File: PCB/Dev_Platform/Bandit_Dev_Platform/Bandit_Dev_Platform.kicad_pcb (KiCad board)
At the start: 4 copper layers, 63.5 x 31.8 mm, 136 parts, among them J1 Conn_01x03_Pin, J10 Conn_01x05_Pin, J11 Conn_01x05_Pin, J2 SMA, J3 Conn_01x05_Pin, J4 Conn_01x05_Pin, J5 BNC, J6 BNC, J8 Conn_01x05_Pin, J9 Conn_01x06_Pin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

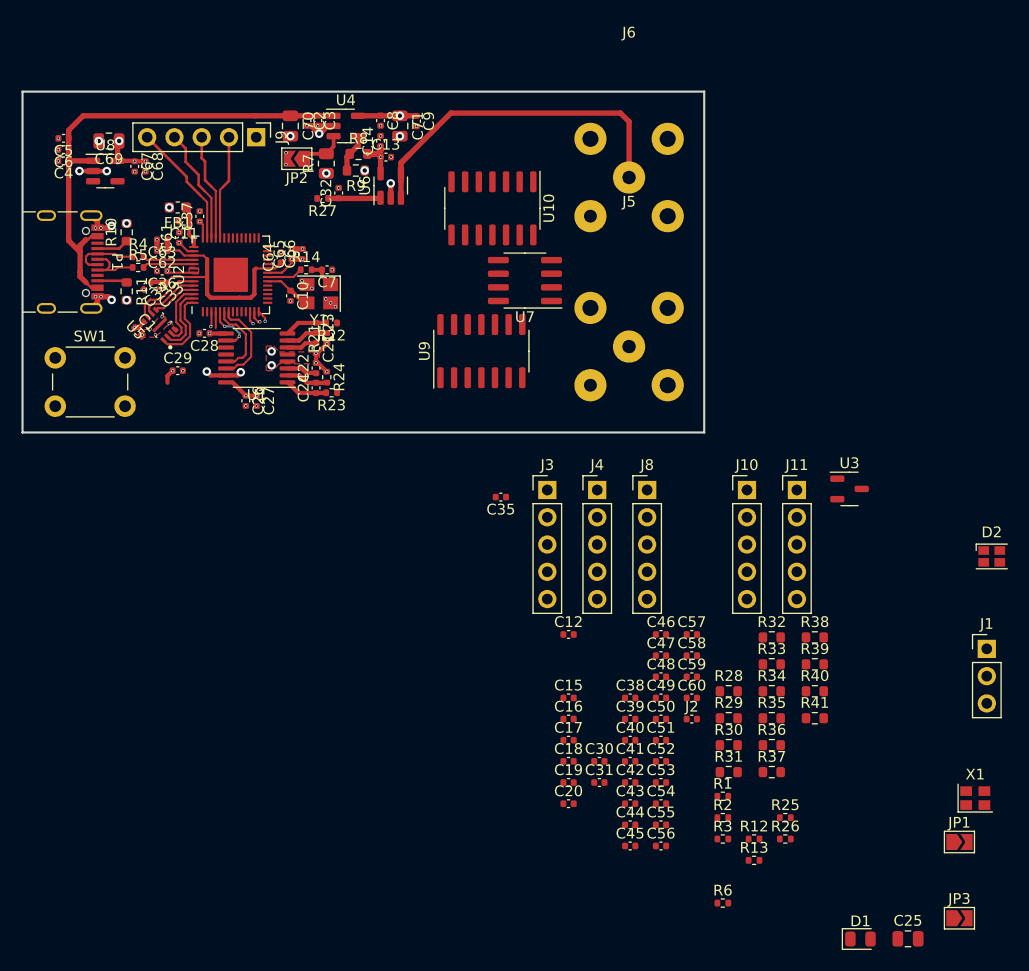
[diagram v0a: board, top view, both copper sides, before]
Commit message: Added circular buffer test, library otw
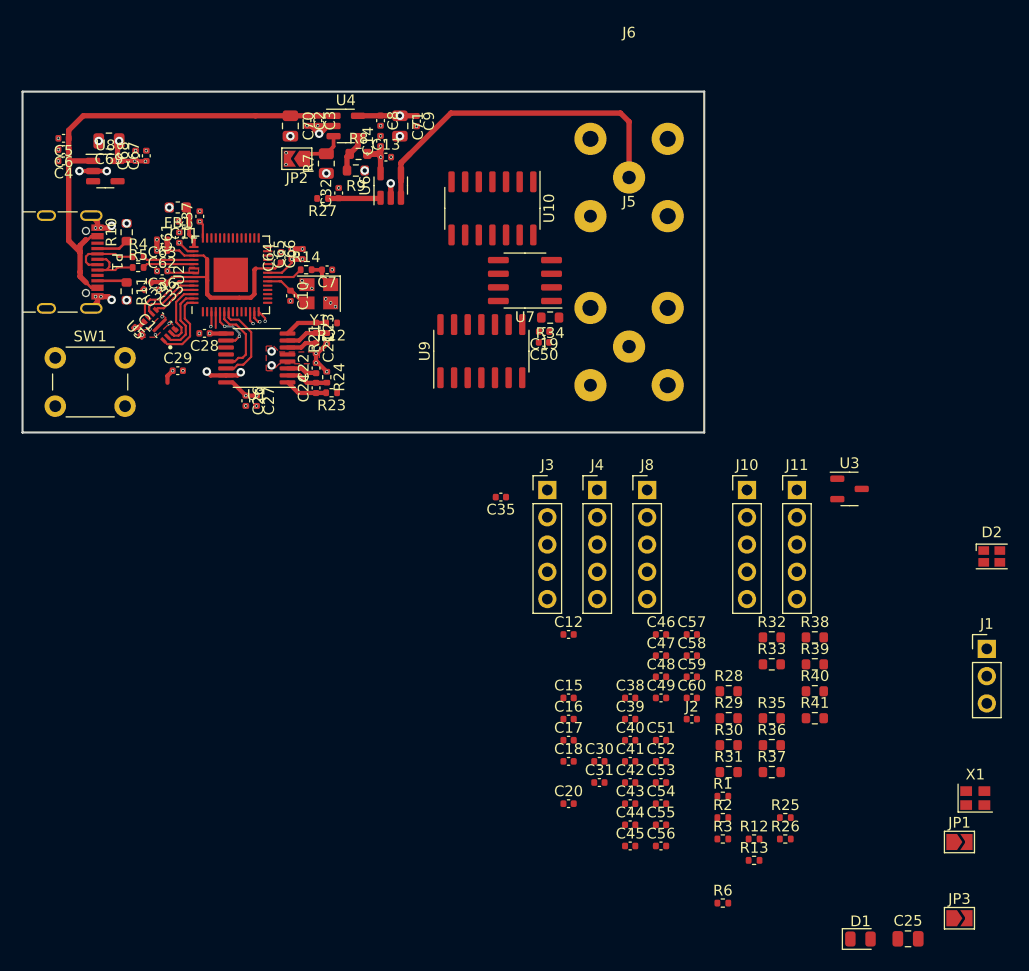
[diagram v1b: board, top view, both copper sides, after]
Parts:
- removed J9: Conn_01x06_Pin, Connector_PinHeader_2.54mm:PinHeader_1x05_P2.54mm_Vertical
- moved C19 42.1 mm to (68.6, 42.4), turned to 180 degrees
- moved R34 40.5 mm to (69.2, 41.0), turned to 180 degrees
- moved C50 36.7 mm to (68.6, 43.4), turned to 180 degrees
- moved C67 1.47 mm to (31.5, 26.0), turned to 90 degrees
- moved C68 1.35 mm to (30.5, 26.0), turned to 90 degrees
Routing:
- net Net-(J9-Pin_5): track 11.7 -> 0.00 mm
- net Net-(J9-Pin_4): track 10.8 -> 0.00 mm
- net Net-(J9-Pin_3): track 9.92 -> 0.00 mm
- net Net-(J9-Pin_2): track 9.73 -> 0.00 mm

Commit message: Circular buffers added to RP2040 evaluation stack
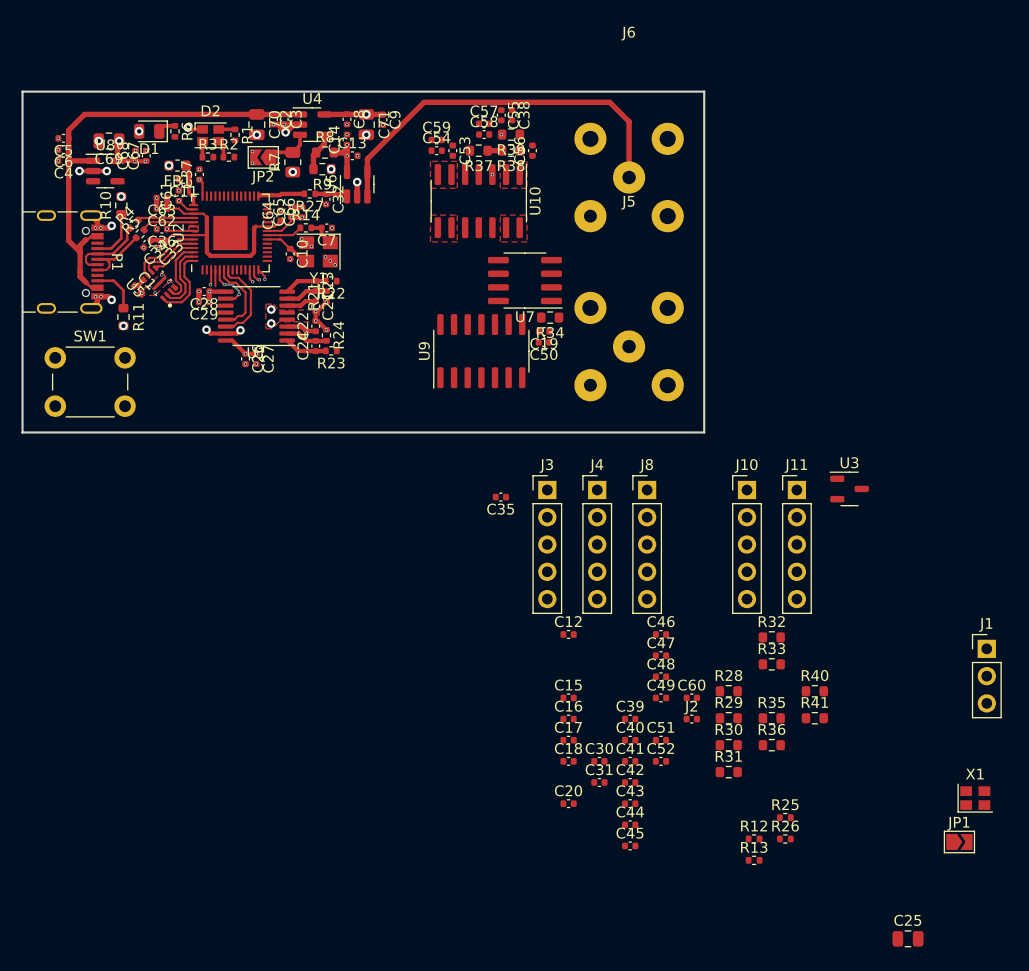
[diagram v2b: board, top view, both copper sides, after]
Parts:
- removed JP3: SolderJumper_2_Open, Jumper:SolderJumper-2_P1.3mm_Open_TrianglePad1.0x1.5mm
- moved D1 100.2 mm to (31.8, 23.7), turned to 180 degrees
- moved R6 88.2 mm to (34.2, 23.7), turned to -90 degrees
- moved D2 82.7 mm to (37.5, 24.1)
- moved R3 79.6 mm to (37.3, 26.1)
- moved R2 76.8 mm to (39.2, 26.1)
- moved R1 76.6 mm to (39.8, 24.0), turned to -90 degrees
- moved C55 67.8 mm to (64.6, 22.2), turned to -90 degrees
- moved C56 65.9 mm to (67.5, 25.5), turned to 90 degrees
- moved C54 64.3 mm to (58.6, 25.5)
- moved R37 64.0 mm to (62.5, 25.5), turned to 180 degrees
- moved C53 62.0 mm to (60.1, 25.5), turned to -90 degrees
- moved R39 56.9 mm to (65.5, 24.0), turned to 180 degrees
- moved C38 55.4 mm to (65.6, 22.2), turned to -90 degrees
- moved C59 55.4 mm to (58.6, 24.5)
- moved R38 53.4 mm to (65.5, 25.5), turned to 180 degrees
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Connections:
- P1 pad B6: (no net) -> Net-(P1-D+)
- P1 pad B7: (no net) -> Net-(P1-D-)
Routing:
- net /PDM_WGN: track 0.00 -> 4.32 mm
- net VBUS: track 46.0 -> 43.0 mm
- net /WGN_OUT: track 33.1 -> 36.0 mm
- net Net-(U6-VIN+): track 4.92 -> 3.05 mm
- net /USB_CC: track 3.01 -> 4.86 mm
- net Net-(D1-K): track 0.00 -> 1.67 mm
- net /USB_VCONN: track 2.78 -> 4.45 mm
- net Net-(D2-GK): track 0.00 -> 1.66 mm
- net Net-(D2-BK): track 0.00 -> 1.53 mm
- net Net-(D2-RK): track 0.00 -> 1.48 mm
- net Net-(C54-Pad2): track 0.00 -> 1.35 mm
- net Net-(P1-D-): track 6.24 -> 7.38 mm
- net +3V3: track 18.3 -> 19.4 mm, vias 15 -> 17
- net Net-(P1-D+): track 6.27 -> 7.33 mm
- net GND: track 21.2 -> 22.2 mm
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- added copper zone on F.Cu, net /SE_SIG_A
- added copper zone on F.Cu, net Net-(U10A--)
- added copper zone on F.Cu, net Net-(U10B--)
- added copper zone on F.Cu, net Net-(U10D--)

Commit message: Fixed filter to be cheap
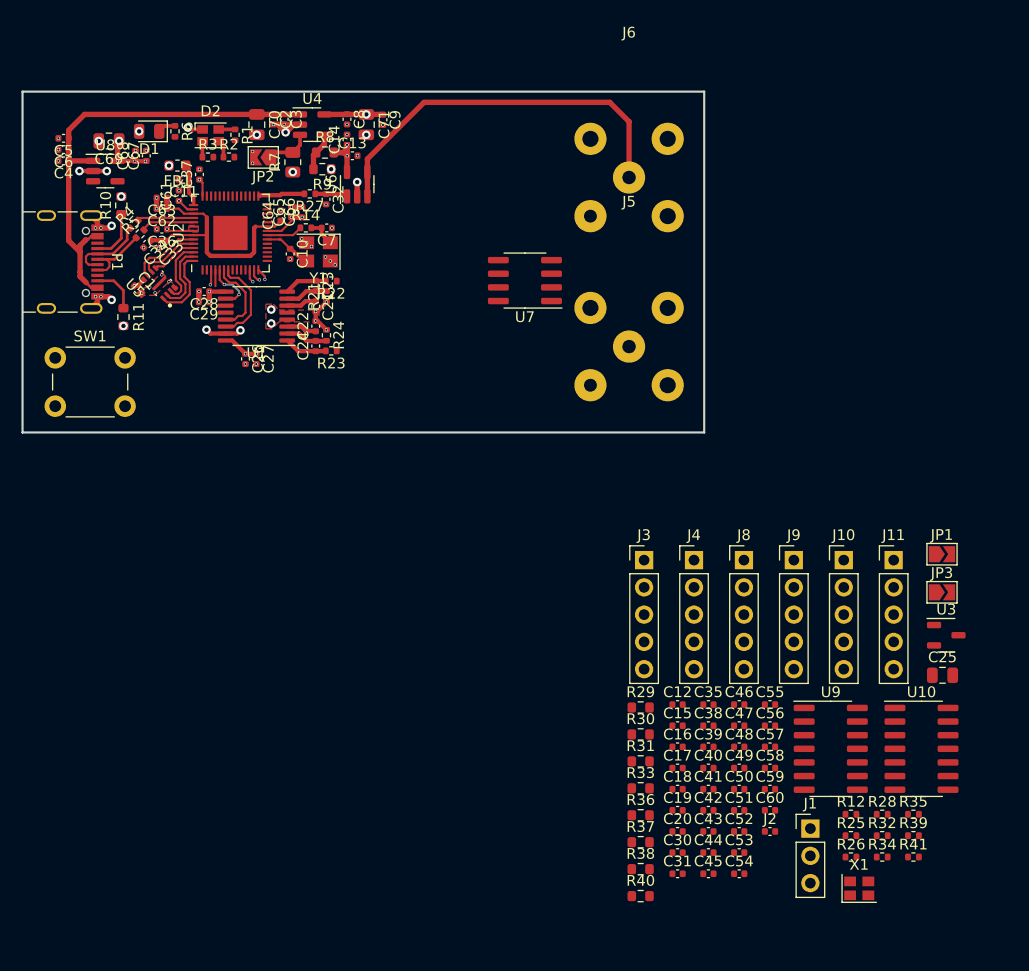
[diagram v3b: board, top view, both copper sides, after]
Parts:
- removed R13: 200R, Resistor_SMD:R_0402_1005Metric
- added J9: Conn_01x06_Pin, Connector_PinHeader_2.54mm:PinHeader_1x05_P2.54mm_Vertical, F.Cu at (91.8, 63.6)
- added JP3: SolderJumper_2_Open, Jumper:SolderJumper-2_P1.3mm_Open_TrianglePad1.0x1.5mm, F.Cu at (105.7, 66.6)
- C16, C19, C20, C38, C41, C46, C50, C55: value 68p C0G -> 33p C0G
- C39, C40: value 330p C0G -> 100p C0G
- C43, C52: value 330p C0G -> 220p C0G
- C45, C54: value 150p C0G -> 100p C0G
- C59, C60: value 150p C0G -> 47p C0G
- R28, R35: value 15k1 -> 15k; footprint Resistor_SMD:R_0603_1608Metric -> Resistor_SMD:R_0402_1005Metric
- R29, R36: value 8k4 -> 8k2
- R30, R37: value 15k2 -> 15k
- R31, R38: value 5k9 -> 5k6
- R32, R39: value 14k8 -> 15k; footprint Resistor_SMD:R_0603_1608Metric -> Resistor_SMD:R_0402_1005Metric
- R33, R40: value 6k3 -> 6k2
- R34, R41: value 11k7 -> 12k; footprint Resistor_SMD:R_0603_1608Metric -> Resistor_SMD:R_0402_1005Metric
- moved R39 75.3 mm to (103.0, 89.3), turned to 0 degrees
- moved C54 73.0 mm to (86.8, 92.9)
- moved C53 70.6 mm to (86.8, 90.9), turned to 0 degrees
- moved R38 68.0 mm to (77.6, 92.4), turned to 0 degrees
- moved C59 68.0 mm to (89.6, 85.0)
- moved R37 66.2 mm to (77.6, 89.9), turned to 0 degrees
- moved U10 65.6 mm to (103.7, 81.2), turned to 0 degrees
- moved C58 64.7 mm to (89.6, 83.0)
- moved C57 63.9 mm to (89.6, 81.0)
- moved C55 60.3 mm to (89.6, 77.1), turned to 0 degrees
- moved C38 59.7 mm to (83.9, 79.1), turned to 0 degrees
- moved R34 59.0 mm to (100.1, 91.3), turned to 0 degrees
- moved C56 58.0 mm to (89.6, 79.1), turned to 0 degrees
- moved U9 49.3 mm to (95.3, 81.2), turned to 0 degrees
- moved C19 46.3 mm to (81.0, 87.0), turned to 0 degrees
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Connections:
- C12 pad 2: GNDA -> GND
- C13 pad 2: GNDA -> GND
- C14 pad 2: GNDA -> GND
- C15 pad 2: GNDA -> GND
- C16 pad 1: GNDA -> GND
- C19 pad 1: GNDA -> GND
- C20 pad 1: GNDA -> GND
- C21 pad 2: GNDA -> GND
- C22 pad 2: GNDA -> GND
- C26 pad 2: GNDA -> GND
- C27 pad 2: GNDA -> GND
- C30 pad 2: GNDA -> GND
- C31 pad 2: GNDA -> GND
- C38 pad 1: GNDA -> GND
- C41 pad 1: GNDA -> GND
- C42 pad 1: GNDA -> GND
- C44 pad 1: GNDA -> GND
- C46 pad 1: GNDA -> GND
- C48 pad 2: GNDA -> GND
- C49 pad 2: GNDA -> GND
- C50 pad 1: GNDA -> GND
- C51 pad 1: GNDA -> GND
- C53 pad 1: GNDA -> GND
- C55 pad 1: GNDA -> GND
- C57 pad 2: GNDA -> GND
- C58 pad 2: GNDA -> GND
- C71 pad 2: GNDA -> GND
- C8 pad 2: GNDA -> GND
- C9 pad 2: GNDA -> GND
- J10 pad 1: GNDA -> GND
- J10 pad 2: GNDA -> GND
- J10 pad 4: GNDA -> GND
- J10 pad 5: GNDA -> GND
- J11 pad 4: GNDA -> GND
- J11 pad 5: GNDA -> GND
- J2 pad 2: GNDA -> GND
- J3 pad 1: GNDA -> GND
- J3 pad 2: GNDA -> GND
- J3 pad 4: GNDA -> GND
- J3 pad 5: GNDA -> GND
- J4 pad 4: GNDA -> GND
- J4 pad 5: GNDA -> GND
- J5 pad 2: GNDA -> GND
- J6 pad 2: GNDA -> GND
- P1 pad B6: Net-(P1-D+) -> (no net)
- P1 pad B7: Net-(P1-D-) -> (no net)
- R21 pad 1: GNDA -> GND
- R24 pad 1: GNDA -> GND
- R26 pad 2: GNDA -> GND
- R9 pad 1: GNDA -> GND
- U1 pad 4: GNDA -> GND
- U1 pad 5: GNDA -> GND
- U10 pad 11: GNDA -> GND
- U6 pad 2: GNDA -> GND
- U7 pad 4: GNDA -> GND
- U9 pad 11: GNDA -> GND
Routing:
- net GND: track 22.2 -> 28.6 mm, vias 50 -> 65
- net GNDA: track 4.93 -> 0.00 mm, vias 15 -> 0
- net Net-(C54-Pad2): track 1.35 -> 0.00 mm
- net Net-(U10A-+): vias 2 -> 0
- removed copper zone on F.Cu, net /SE_SIG_A
- removed copper zone on F.Cu, net GNDA
- removed copper zone on In2.Cu, net GNDA
- removed copper zone on F.Cu, net Net-(U10A--)
- removed copper zone on F.Cu, net Net-(U10B--)
- removed copper zone on F.Cu, net Net-(U10D--)

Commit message: PCB stuff
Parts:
- moved C54 74.5 mm to (58.4, 24.0), turned to 90 degrees
- moved R39 73.8 mm to (67.0, 24.9), turned to 90 degrees
- moved C53 71.5 mm to (61.8, 24.0), turned to -90 degrees
- moved R38 70.0 mm to (65.8, 23.4), turned to 90 degrees
- moved R41 69.4 mm to (65.1, 33.2), turned to 90 degrees
- moved R35 68.8 mm to (60.4, 33.2), turned to 90 degrees
- moved R37 68.7 mm to (60.6, 23.4), turned to -90 degrees
- moved C59 68.2 mm to (59.3, 24.0), turned to 90 degrees
- moved U10 67.2 mm to (62.0, 28.6), turned to -90 degrees
- moved R40 66.3 mm to (67.4, 29.4), turned to 90 degrees
- moved R36 62.9 mm to (56.6, 28.1), turned to -90 degrees
- moved C52 62.0 mm to (59.5, 33.2), turned to -90 degrees
- moved C51 59.5 mm to (61.4, 33.2), turned to 90 degrees
- moved C55 58.9 mm to (64.3, 24.0), turned to -90 degrees
- moved C38 58.8 mm to (63.3, 23.9), turned to -90 degrees
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
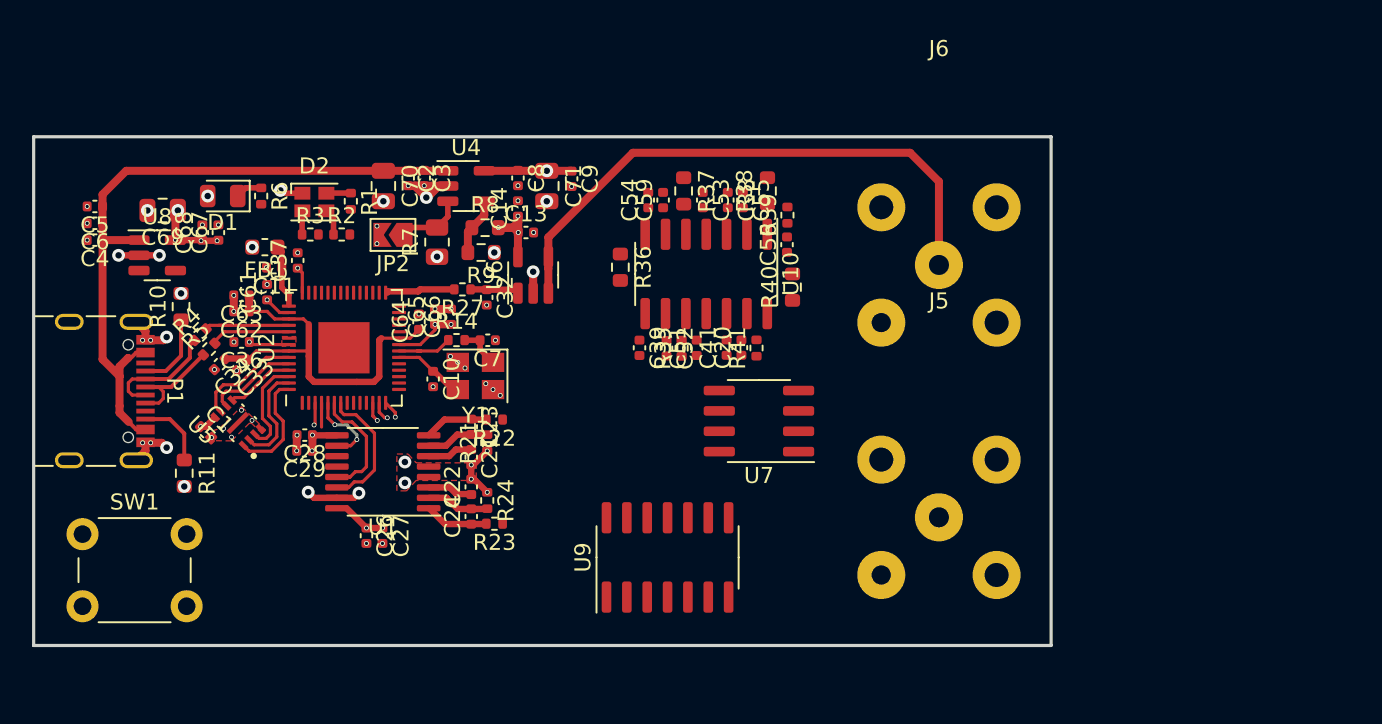
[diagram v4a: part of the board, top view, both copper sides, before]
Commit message: Fixed BNC issue, changed more parts to be free.99
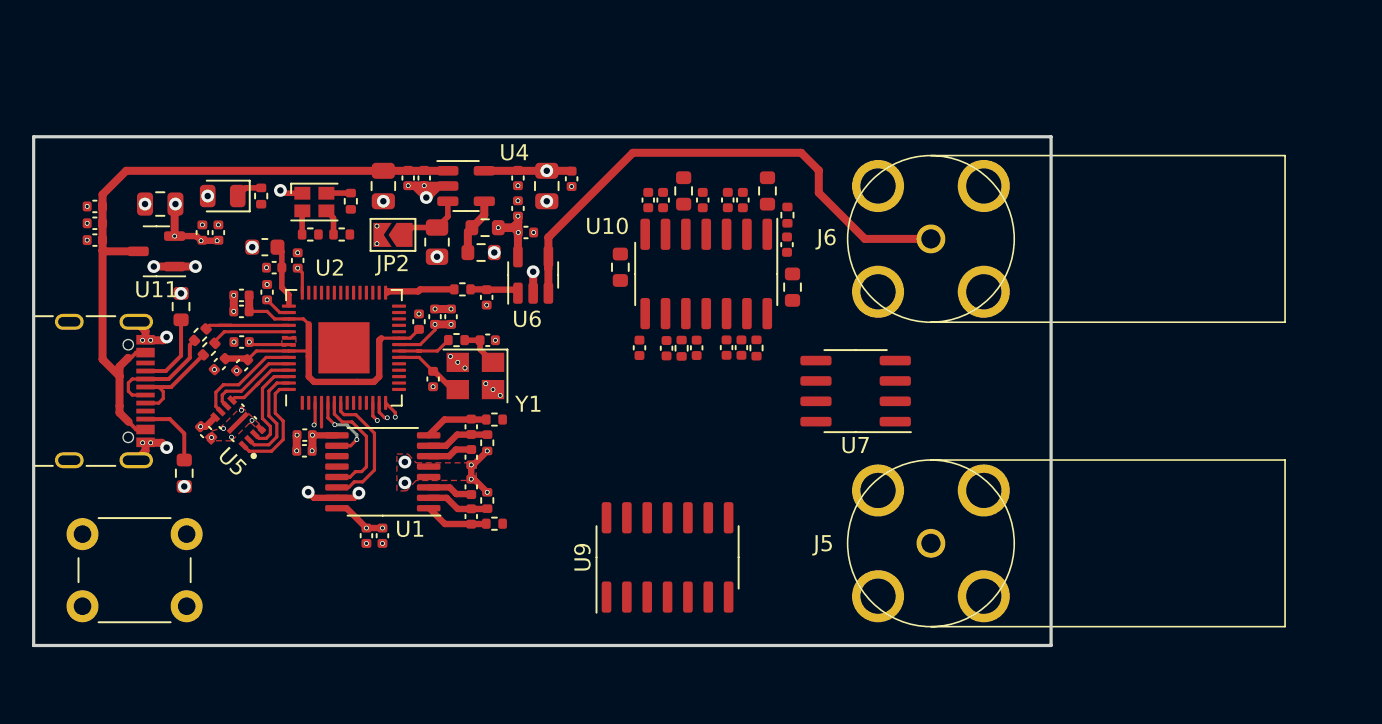
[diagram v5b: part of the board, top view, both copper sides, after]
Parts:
- removed U8: MIC5504-3.3YM5, Package_TO_SOT_SMD:SOT-23-5
- added U11: XC6206PxxxMR, Package_TO_SOT_SMD:SOT-23-3, F.Cu at (27.7, 27.1)
- J5, J6: footprint ADS8584SIPM:BNC_THT -> BANDIT_PCB_Lib:DOSIN-801-0050
- moved U7 6.32 mm to (71.3, 35.9)
- moved J5 1.70 mm to (76.0, 45.4)
- moved J6 1.70 mm to (76.0, 26.4)
- moved C69 0.43 mm to (27.9, 24.2)
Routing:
- net /WGN_OUT: track 36.0 -> 32.6 mm

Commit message: Almost done w pcb
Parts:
- moved R34 64.1 mm to (63.7, 38.5), turned to 180 degrees
- moved R28 64.0 mm to (58.5, 38.7), turned to -90 degrees
- moved C58 63.9 mm to (60.2, 26.2), turned to 90 degrees
- moved C57 62.7 mm to (59.2, 26.2), turned to 90 degrees
- moved R26 57.7 mm to (77.6, 37.0), turned to -90 degrees
- moved C43 57.1 mm to (56.7, 38.7), turned to 90 degrees
- moved R25 55.5 mm to (78.7, 37.0), turned to 90 degrees
- moved R32 54.9 mm to (65.0, 47.1), turned to -90 degrees
- moved C42 54.0 mm to (59.5, 38.7), turned to -90 degrees
- moved C45 53.4 mm to (54.7, 48.1), turned to -90 degrees
- moved C40 52.5 mm to (55.7, 38.7), turned to 90 degrees
- moved C50 52.5 mm to (62.2, 38.6), turned to -90 degrees
- moved C19 52.2 mm to (61.2, 38.6), turned to -90 degrees
- moved C60 51.6 mm to (55.7, 48.1), turned to -90 degrees
- moved C44 49.8 mm to (58.3, 48.1), turned to 90 degrees
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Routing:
- net /WGN_OUT: track 32.6 -> 46.5 mm
- net /SE_SIG_A: track 0.00 -> 13.5 mm
- net /SE_SIG_B: track 0.00 -> 13.3 mm
- net /SIG_IN: track 0.00 -> 10.4 mm
- net Net-(C45-Pad2): track 0.00 -> 9.72 mm
- net Net-(C54-Pad2): track 0.00 -> 9.41 mm
- net VDDA: track 13.5 -> 22.2 mm, vias 6 -> 11
- net GND: track 28.6 -> 37.1 mm, vias 65 -> 86
- net Net-(C39-Pad2): track 0.00 -> 7.95 mm, vias 0 -> 2
- net Net-(C40-Pad2): track 0.00 -> 7.76 mm, vias 0 -> 2
- net Net-(J2-In): track 0.00 -> 6.97 mm
- net Net-(U9A--): track 0.00 -> 6.87 mm
- net Net-(U10B--): track 0.00 -> 6.71 mm
- net Net-(C56-Pad2): track 0.00 -> 6.39 mm
- net Net-(U10A-+): track 0.00 -> 5.45 mm, vias 0 -> 2
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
